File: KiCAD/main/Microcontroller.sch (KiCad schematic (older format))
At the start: 10 parts, among them J6 Conn_02x04_Odd_Even, SW2 BOOT, SW3 RESET, U3 ESP32-WROOM-32

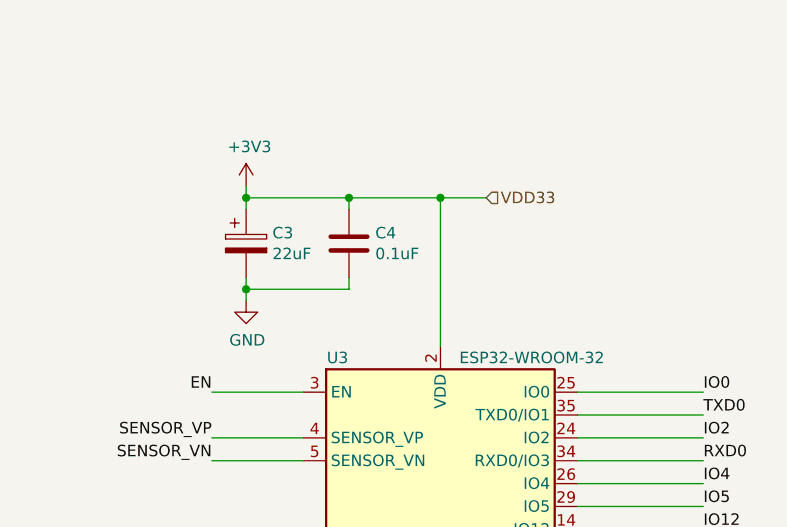
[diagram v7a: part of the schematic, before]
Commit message: Increase margins for the fixtures
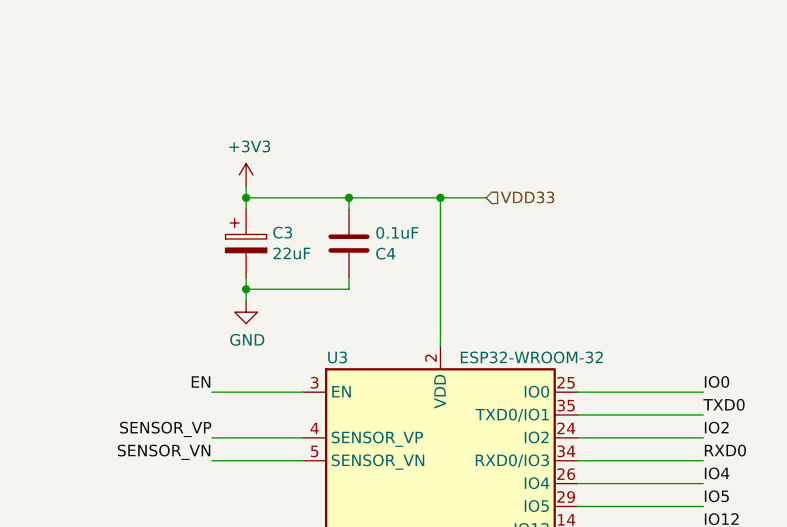
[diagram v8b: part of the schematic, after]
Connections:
- net +3V3: now also C4.2; no longer C4.1
- net GND: now also C4.1; no longer C4.2
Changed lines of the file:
@@
-	1    0    0    -1
-$EndComp
-$Comp
-L Device:C C4
-U 1 1 5F9451F0
-P 7800 1850
-F 0 "C4" H 7915 1896 50  0000 L CNN
-F 1 "0.1uF" H 7915 1805 50  0000 L CNN
-F 2 "Capacitor_THT:C_Disc_D4.3mm_W1.9mm_P5.00mm" H 7838 1700 50  0001 C CNN
-F 3 "~" H 7800 1850 50  0001 C CNN
-F 4 "50V" H 7915 1759 50  0001 L CNN "Voltage"
-	1    7800 1850
 	1    0    0    -1
 $EndComp
@@
 	1    0    0    -1
 $EndComp
+$Comp
+L Device:C C4
+U 1 1 5F9451F0
+P 7800 1850
+F 0 "C4" H 7915 1896 50  0000 L CNN
+F 1 "0.1uF" H 7915 1805 50  0000 L CNN
+F 2 "Capacitor_THT:C_Disc_D4.3mm_W1.9mm_P5.00mm" H 7838 1700 50  0001 C CNN
+F 3 "~" H 7800 1850 50  0001 C CNN
+F 4 "50V" H 7915 1759 50  0001 L CNN "Voltage"
+	1    7800 1850
+	1    0    0    1
+$EndComp
 $EndSCHEMATC
